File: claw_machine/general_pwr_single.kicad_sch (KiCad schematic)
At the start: 6 parts, among them J33 Conn_01x02_Pin, J37 Screw_Terminal_01x02, Q1 AO3400A

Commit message: Rework schematic
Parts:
- removed D1: LED, LED_THT:LED_D1.8mm_W1.8mm_H2.4mm_Horizontal_O1.27mm_Z1.6mm, symbol Device:LED
- removed J33: Conn_01x02_Pin, symbol Connector:Conn_01x02_Pin
- added D6: LED, LED_THT:LED_D1.8mm_W1.8mm_H2.4mm_Horizontal_O1.27mm_Z1.6mm, symbol Device:LED
- added J28: Conn_01x02, symbol Connector_Generic:Conn_01x02
- added R17: 2k2, Resistor_SMD:R_0805_2012Metric_Pad1.20x1.40mm_HandSolder, symbol Device:R
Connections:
- net GND: now also Q1.2 (S), R17.2, R17.2
- net at J37.2 (Pin_2), Q1.3 (D): now also J28.2 (Pin_2)
- net at J37.1 (Pin_1), JP1.2 (C): now also J28.1 (Pin_1)
- net pwr_input renamed EN
- net EN: now also D6.2 (A)
- new net: D6.1 (K), R17.1
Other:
- note added: "Active High Control"
- moved on the sheet: J37, JP1, Q1, R17

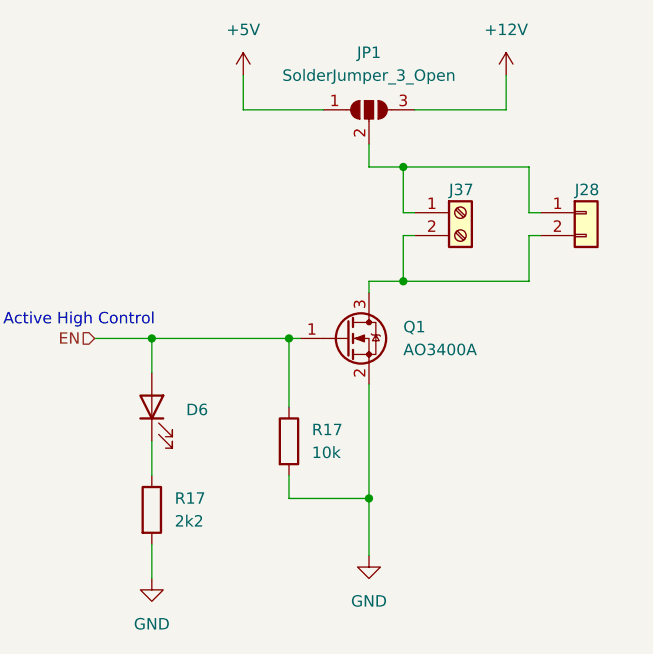
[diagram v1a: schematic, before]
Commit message: Assign footprints
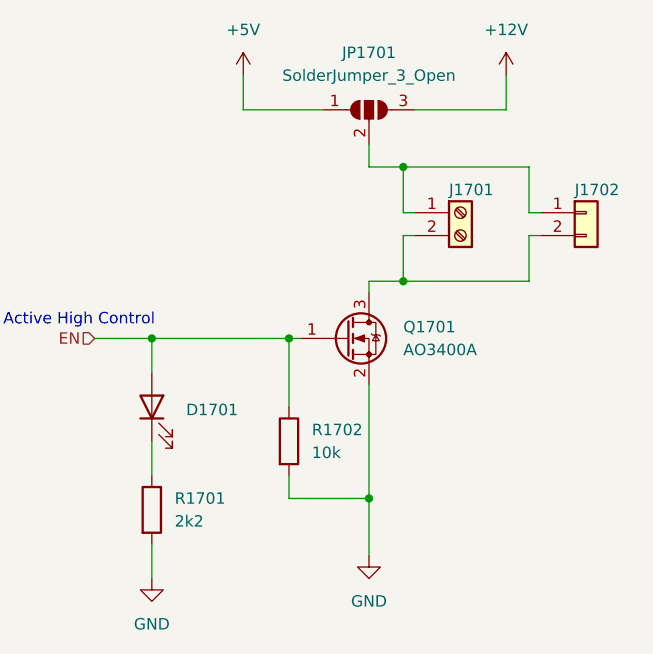
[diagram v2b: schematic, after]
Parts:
- D1701: renamed from D6; footprint LED_THT:LED_D1.8mm_W1.8mm_H2.4mm_Horizontal_O1.27mm_Z1.6mm -> LED_SMD:LED_1206_3216Metric_Pad1.42x1.75mm_HandSolder
- J1701: renamed from J37; footprint (none) -> TerminalBlock:TerminalBlock_bornier-2_P5.08mm
- J1702: renamed from J28; footprint (none) -> Connector_PinHeader_2.54mm:PinHeader_1x02_P2.54mm_Vertical
- R1701, R1702: renamed from R17; footprint Resistor_SMD:R_0805_2012Metric_Pad1.20x1.40mm_HandSolder -> Resistor_SMD:R_1206_3216Metric_Pad1.30x1.75mm_HandSolder
- renumbered JP1 to JP1701, Q1 to Q1701
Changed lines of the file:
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@@
   (symbol (lib_id "Transistor_FET:AO3400A") (at 73.66 63.5 0) (unit 1)
     (in_bom yes) (on_board yes) (dnp no) (fields_autoplaced)
-    (property "Reference" "Q1" (at 80.01 62.23 0)
+    (property "Reference" "Q1701" (at 80.01 62.23 0)
       (effects (font (size 1.27 1.27)) (justify left))
     )
@@
   (symbol (lib_id "power:GND") (at 76.2 87.63 0) (unit 1)
     (in_bom yes) (on_board yes) (dnp no) (fields_autoplaced)
-    (property "Reference" "#PWR049" (at 76.2 93.98 0)
+    (property "Reference" "#PWR01703" (at 76.2 93.98 0)
       (effects (font (size 1.27 1.27)) hide)
     )
@@
   (symbol (lib_id "Device:R") (at 52.07 82.55 0) (unit 1)
     (in_bom yes) (on_board yes) (dnp no) (fields_autoplaced)
-    (property "Reference" "R17" (at 54.61 81.28 0)
+    (property "Reference" "R1701" (at 54.61 81.28 0)
       (effects (font (size 1.27 1.27)) (justify left))
     )
@@
       (effects (font (size 1.27 1.27)) (justify left))
     )
-    (property "Footprint" "Resistor_SMD:R_0805_2012Metric_Pad1.20x1.40mm_HandSolder" (at 50.292 82.55 90)
+    (property "Footprint" "Resistor_SMD:R_1206_3216Metric_Pad1.30x1.75mm_HandSolder" (at 50.292 82.55 90)
       (effects (font (size 1.27 1.27)) hide)
     )
@@
   (symbol (lib_id "Connector_Generic:Conn_01x02") (at 100.33 49.53 0) (unit 1)
     (in_bom yes) (on_board yes) (dnp no)
-    (property "Reference" "J28" (at 99.06 46.99 0)
+    (property "Reference" "J1702" (at 99.06 46.99 0)
       (effects (font (size 1.27 1.27)) (justify left))
     )
@@
       (effects (font (size 1.27 1.27)) (justify left) hide)
     )
-    (property "Footprint" "" (at 100.33 49.53 0)
+    (property "Footprint" "Connector_PinHeader_2.54mm:PinHeader_1x02_P2.54mm_Vertical" (at 100.33 49.53 0)
       (effects (font (size 1.27 1.27)) hide)
     )
@@
   (symbol (lib_id "Connector:Screw_Terminal_01x02") (at 86.36 49.53 0) (unit 1)
     (in_bom yes) (on_board yes) (dnp no)
-    (property "Reference" "J37" (at 85.09 46.99 0)
+    (property "Reference" "J1701" (at 85.09 46.99 0)
       (effects (font (size 1.27 1.27)) (justify left))
     )
@@
       (effects (font (size 1.27 1.27)) (justify left) hide)
     )
-    (property "Footprint" "" (at 86.36 49.53 0)
+    (property "Footprint" "TerminalBlock:TerminalBlock_bornier-2_P5.08mm" (at 86.36 49.53 0)
       (effects (font (size 1.27 1.27)) hide)
     )
@@
   (symbol (lib_id "power:+12V") (at 91.44 34.29 0) (unit 1)
     (in_bom yes) (on_board yes) (dnp no) (fields_autoplaced)
-    (property "Reference" "#PWR050" (at 91.44 38.1 0)
+    (property "Reference" "#PWR01704" (at 91.44 38.1 0)
       (effects (font (size 1.27 1.27)) hide)
     )
@@
   (symbol (lib_id "Device:LED") (at 52.07 71.12 90) (unit 1)
     (in_bom yes) (on_board yes) (dnp no) (fields_autoplaced)
-    (property "Reference" "D6" (at 55.88 71.4375 90)
+    (property "Reference" "D1701" (at 55.88 71.4375 90)
       (effects (font (size 1.27 1.27)) (justify right))
     )
@@
       (effects (font (size 1.27 1.27)) (justify right) hide)
     )
-    (property "Footprint" "LED_THT:LED_D1.8mm_W1.8mm_H2.4mm_Horizontal_O1.27mm_Z1.6mm" (at 52.07 71.12 0)
+    (property "Footprint" "LED_SMD:LED_1206_3216Metric_Pad1.42x1.75mm_HandSolder" (at 52.07 71.12 0)
       (effects (font (size 1.27 1.27)) hide)
     )
@@
   (symbol (lib_id "power:+5V") (at 62.23 34.29 0) (unit 1)
     (in_bom yes) (on_board yes) (dnp no) (fields_autoplaced)
-    (property "Reference" "#PWR048" (at 62.23 38.1 0)
+    (property "Reference" "#PWR01702" (at 62.23 38.1 0)
       (effects (font (size 1.27 1.27)) hide)
     )
@@
   (symbol (lib_id "power:GND") (at 52.07 90.17 0) (unit 1)
     (in_bom yes) (on_board yes) (dnp no) (fields_autoplaced)
-    (property "Reference" "#PWR049" (at 52.07 96.52 0)
+    (property "Reference" "#PWR01701" (at 52.07 96.52 0)
       (effects (font (size 1.27 1.27)) hide)
     )
@@
   (symbol (lib_id "Jumper:SolderJumper_3_Open") (at 76.2 38.1 0) (unit 1)
     (in_bom yes) (on_board yes) (dnp no) (fields_autoplaced)
-    (property "Reference" "JP1" (at 76.2 31.75 0)
+    (property "Reference" "JP1701" (at 76.2 31.75 0)
       (effects (font (size 1.27 1.27)))
     )
@@
   (symbol (lib_id "Device:R") (at 67.31 74.93 0) (unit 1)
     (in_bom yes) (on_board yes) (dnp no) (fields_autoplaced)
-    (property "Reference" "R17" (at 69.85 73.66 0)
+    (property "Reference" "R1702" (at 69.85 73.66 0)
       (effects (font (size 1.27 1.27)) (justify left))
     )
@@
       (effects (font (size 1.27 1.27)) (justify left))
     )
-    (property "Footprint" "Resistor_SMD:R_0805_2012Metric_Pad1.20x1.40mm_HandSolder" (at 65.532 74.93 90)
-      (effects (font (size 1.27 1.27)) hide)
-    )
+    (property "Footprint" "Resistor_SMD:R_1206_3216Metric_Pad1.30x1.75mm_HandSolder" (at 65.532 74.93 90)
+      (effects (font (size 1.27 1.27)) hide)
+    )

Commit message: Route all power traced and replicated sections
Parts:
- Q1701: footprint Package_TO_SOT_SMD:SOT-23 -> Library:SOT-23-MassivePads-HandSolder
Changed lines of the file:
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@@
       (effects (font (size 1.27 1.27)) (justify left))
     )
-    (property "Footprint" "Package_TO_SOT_SMD:SOT-23" (at 78.74 65.405 0)
+    (property "Footprint" "Library:SOT-23-MassivePads-HandSolder" (at 78.74 65.405 0)
       (effects (font (size 1.27 1.27) italic) (justify left) hide)
     )

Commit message: Minor change reconcile
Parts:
- JP1701: footprint Jumper:SolderJumper-3_P1.3mm_Open_Pad1.0x1.5mm_NumberLabels -> Jumper:SolderJumper-3_P1.3mm_Open_RoundedPad1.0x1.5mm_NumberLabels
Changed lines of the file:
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@@
       (effects (font (size 1.27 1.27)))
     )
-    (property "Footprint" "Jumper:SolderJumper-3_P1.3mm_Open_Pad1.0x1.5mm_NumberLabels" (at 76.2 38.1 0)
+    (property "Footprint" "Jumper:SolderJumper-3_P1.3mm_Open_RoundedPad1.0x1.5mm_NumberLabels" (at 76.2 38.1 0)
       (effects (font (size 1.27 1.27)) hide)
     )
